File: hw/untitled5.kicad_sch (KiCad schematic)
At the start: 1 part, among them U6 TS3USB3031

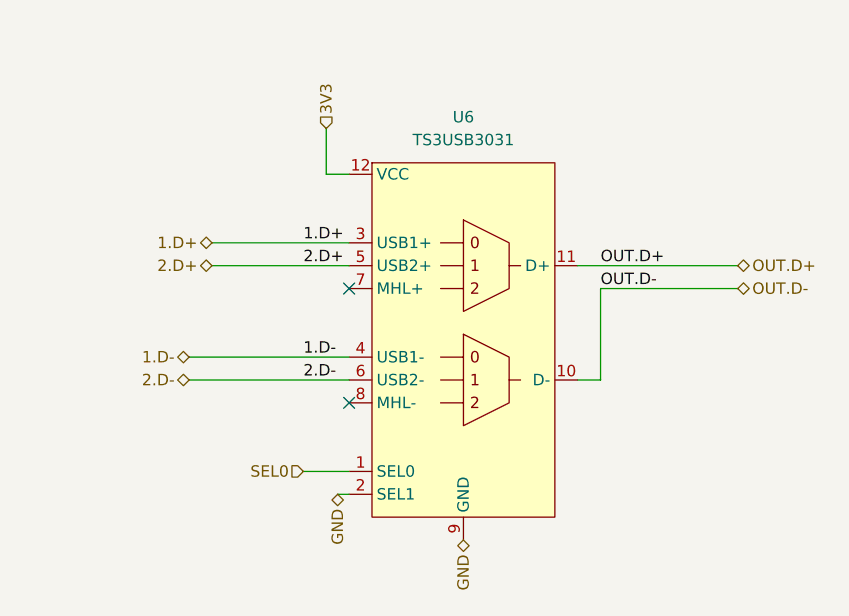
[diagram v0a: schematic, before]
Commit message: Graphic modifications of the scheme
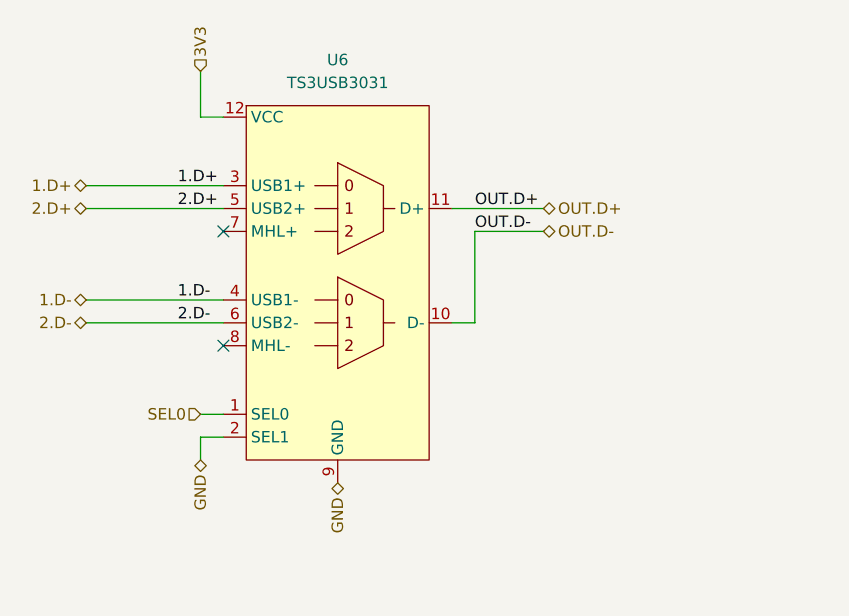
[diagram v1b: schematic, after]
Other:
- moved on the sheet: U6
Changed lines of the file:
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@@
 (kicad_sch (version 20230121) (generator eeschema)
   (paper "A4")
-  (no_connect (at 156.21 87.63))
-  (no_connect (at 156.21 100.33))
-  (wire (pts (xy 140.97 85.09) (xy 156.21 85.09))
+  (no_connect (at 142.24 81.28))
+  (no_connect (at 142.24 93.98))
+  (wire (pts (xy 139.7 106.68) (xy 139.7 104.14))
     (stroke (width 0) (type default))
   )
-  (wire (pts (xy 156.21 74.93) (xy 153.67 74.93))
+  (wire (pts (xy 127 78.74) (xy 142.24 78.74))
     (stroke (width 0) (type default))
   )
-  (wire (pts (xy 154.94 110.49) (xy 156.21 110.49))
+  (wire (pts (xy 142.24 68.58) (xy 139.7 68.58))
     (stroke (width 0) (type default))
   )
-  (wire (pts (xy 138.43 97.79) (xy 156.21 97.79))
+  (wire (pts (xy 127 91.44) (xy 142.24 91.44))
     (stroke (width 0) (type default))
   )
-  (wire (pts (xy 181.61 85.09) (xy 199.39 85.09))
+  (wire (pts (xy 167.64 78.74) (xy 177.8 78.74))
     (stroke (width 0) (type default))
   )
-  (wire (pts (xy 184.15 87.63) (xy 199.39 87.63))
+  (wire (pts (xy 139.7 104.14) (xy 142.24 104.14))
     (stroke (width 0) (type default))
   )
-  (wire (pts (xy 181.61 97.79) (xy 184.15 97.79))
+  (wire (pts (xy 170.18 81.28) (xy 177.8 81.28))
     (stroke (width 0) (type default))
   )
-  (wire (pts (xy 151.13 107.95) (xy 156.21 107.95))
+  (wire (pts (xy 167.64 91.44) (xy 170.18 91.44))
     (stroke (width 0) (type default))
   )
-  (wire (pts (xy 138.43 95.25) (xy 156.21 95.25))
+  (wire (pts (xy 139.7 101.6) (xy 142.24 101.6))
     (stroke (width 0) (type default))
   )
-  (wire (pts (xy 184.15 97.79) (xy 184.15 87.63))
+  (wire (pts (xy 127 88.9) (xy 142.24 88.9))
     (stroke (width 0) (type default))
   )
-  (wire (pts (xy 140.97 82.55) (xy 156.21 82.55))
+  (wire (pts (xy 170.18 91.44) (xy 170.18 81.28))
     (stroke (width 0) (type default))
   )
-  (wire (pts (xy 153.67 69.85) (xy 153.67 74.93))
+  (wire (pts (xy 127 76.2) (xy 142.24 76.2))
     (stroke (width 0) (type default))
   )
-  (label "1.D+" (at 151.13 82.55 0) (fields_autoplaced)
+  (wire (pts (xy 139.7 63.5) (xy 139.7 68.58))
+    (stroke (width 0) (type default))
+  )
+  (label "1.D+" (at 137.16 76.2 0) (fields_autoplaced)
     (effects (font (size 1.27 1.27)) (justify left bottom))
   )
-  (label "1.D-" (at 151.13 95.25 0) (fields_autoplaced)
+  (label "1.D-" (at 137.16 88.9 0) (fields_autoplaced)
     (effects (font (size 1.27 1.27)) (justify left bottom))
   )
-  (label "OUT.D-" (at 184.15 87.63 0) (fields_autoplaced)
+  (label "OUT.D-" (at 170.18 81.28 0) (fields_autoplaced)
     (effects (font (size 1.27 1.27)) (justify left bottom))
   )
-  (label "2.D-" (at 151.13 97.79 0) (fields_autoplaced)
+  (label "2.D-" (at 137.16 91.44 0) (fields_autoplaced)
     (effects (font (size 1.27 1.27)) (justify left bottom))
   )
-  (label "OUT.D+" (at 184.15 85.09 0) (fields_autoplaced)
+  (label "OUT.D+" (at 170.18 78.74 0) (fields_autoplaced)
     (effects (font (size 1.27 1.27)) (justify left bottom))
   )
-  (label "2.D+" (at 151.13 85.09 0) (fields_autoplaced)
+  (label "2.D+" (at 137.16 78.74 0) (fields_autoplaced)
     (effects (font (size 1.27 1.27)) (justify left bottom))
   )
-  (hierarchical_label "2.D-" (shape bidirectional) (at 138.43 97.79 180) (fields_autoplaced)
+  (hierarchical_label "2.D-" (shape bidirectional) (at 127 91.44 180) (fields_autoplaced)
     (effects (font (size 1.27 1.27)) (justify right))
   )
-  (hierarchical_label "3V3" (shape input) (at 153.67 69.85 90) (fields_autoplaced)
+  (hierarchical_label "3V3" (shape input) (at 139.7 63.5 90) (fields_autoplaced)
     (effects (font (size 1.27 1.27)) (justify left))
   )
-  (hierarchical_label "1.D-" (shape bidirectional) (at 138.43 95.25 180) (fields_autoplaced)
+  (hierarchical_label "1.D-" (shape bidirectional) (at 127 88.9 180) (fields_autoplaced)
     (effects (font (size 1.27 1.27)) (justify right))
   )
-  (hierarchical_label "2.D+" (shape bidirectional) (at 140.97 85.09 180) (fields_autoplaced)
+  (hierarchical_label "2.D+" (shape bidirectional) (at 127 78.74 180) (fields_autoplaced)
     (effects (font (size 1.27 1.27)) (justify right))
   )
-  (hierarchical_label "GND" (shape bidirectional) (at 168.91 115.57 270) (fields_autoplaced)
+  (hierarchical_label "GND" (shape bidirectional) (at 154.94 109.22 270) (fields_autoplaced)
     (effects (font (size 1.27 1.27)) (justify right))
   )
-  (hierarchical_label "OUT.D+" (shape bidirectional) (at 199.39 85.09 0) (fields_autoplaced)
+  (hierarchical_label "OUT.D+" (shape bidirectional) (at 177.8 78.74 0) (fields_autoplaced)
     (effects (font (size 1.27 1.27)) (justify left))
   )
-  (hierarchical_label "1.D+" (shape bidirectional) (at 140.97 82.55 180) (fields_autoplaced)
+  (hierarchical_label "1.D+" (shape bidirectional) (at 127 76.2 180) (fields_autoplaced)
     (effects (font (size 1.27 1.27)) (justify right))
   )
-  (hierarchical_label "GND" (shape bidirectional) (at 154.94 110.49 270) (fields_autoplaced)
+  (hierarchical_label "GND" (shape bidirectional) (at 139.7 106.68 270) (fields_autoplaced)
     (effects (font (size 1.27 1.27)) (justify right))
   )
-  (hierarchical_label "SEL0" (shape input) (at 151.13 107.95 180) (fields_autoplaced)
+  (hierarchical_label "SEL0" (shape input) (at 139.7 101.6 180) (fields_autoplaced)
     (effects (font (size 1.27 1.27)) (justify right))
   )
-  (hierarchical_label "OUT.D-" (shape bidirectional) (at 199.39 87.63 0) (fields_autoplaced)
+  (hierarchical_label "OUT.D-" (shape bidirectional) (at 177.8 81.28 0) (fields_autoplaced)
     (effects (font (size 1.27 1.27)) (justify left))
   )
-  (symbol (lib_id "RKL-DiscreteLogic:TS3USB3031") (at 168.91 74.93 0) (unit 1)
+  (symbol (lib_id "RKL-DiscreteLogic:TS3USB3031") (at 154.94 68.58 0) (unit 1)
     (in_bom yes) (on_board yes) (dnp no)
-    (property "Reference" "U6" (at 168.91 68.58 0)
+    (property "Reference" "U6" (at 154.94 62.23 0)
       (effects (font (size 1.27 1.27)))
     )
-    (property "Value" "TS3USB3031" (at 168.91 71.12 0)
+    (property "Value" "TS3USB3031" (at 154.94 64.77 0)
       (effects (font (size 1.27 1.27)))
     )
-    (property "Footprint" "Package_DFN_QFN:Texas_X2QFN-12_1.6x1.6mm_P0.4mm" (at 168.91 66.04 0)
+    (property "Footprint" "Package_DFN_QFN:Texas_X2QFN-12_1.6x1.6mm_P0.4mm" (at 154.94 59.69 0)
       (effects (font (size 1.27 1.27)) hide)
     )
-    (property "Datasheet" "https://www.ti.com/lit/ds/symlink/ts3usb3031.pdf?ts=1703029289212&ref_url=https%253A%252F%252Fwww.google.com%252F" (at 168.91 63.5 0)
+    (property "Datasheet" "https://www.ti.com/lit/ds/symlink/ts3usb3031.pdf?ts=1703029289212&ref_url=https%253A%252F%252Fwww.google.com%252F" (at 154.94 57.15 0)
       (effects (font (size 1.27 1.27)) hide)
     )
-    (property "Basic/Extended" "E" (at 168.91 74.93 0)
+    (property "Basic/Extended" "E" (at 154.94 68.58 0)
       (effects (font (size 1.27 1.27)) hide)
     )
-    (property "LCSC" "C2652459" (at 168.91 74.93 0)
+    (property "LCSC" "C2652459" (at 154.94 68.58 0)
       (effects (font (size 1.27 1.27)) hide)
     )

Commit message: add routing
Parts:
- added C2: 4.7u, Capacitor_SMD:C_0603_1608Metric, symbol Device:C
- added C29: 10u, Capacitor_SMD:C_0603_1608Metric, symbol Device:C
- added R40: 10k, Resistor_SMD:R_0402_1005Metric, symbol Device:R
- added R41: 56k, Resistor_SMD:R_0402_1005Metric, symbol Device:R
- added U2: LD39200, Package_DFN_QFN:DFN-8-1EP_4x4mm_P0.8mm_EP2.3x3.24mm, symbol Robotarna_KiCad_Library:LD39200
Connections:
- net GND: now also C2.2, C29.2, R40.1, U2.4 (GND), U2.9 (GND)
- net 3V3: no longer names the net of U6.12 (VCC)
- net 3V3: now also C29.1, R41.2, U2.1 (OUT), U2.2 (OUT)
- new net: R40.2, R41.1, U2.3 (ADJ/SENSE)
- new net IN: C2.1, U2.6 (EN), U2.7 (IN), U2.8 (IN)
- no-connect marks 2 -> 3

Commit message: Component inspection wip 0
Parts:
- C29: Basic/Extended (none) -> B; LCSC C19702 -> C96446; info (none) -> 25V, X5R
- R40: Basic/Extended (none) -> B
- U2: symbol Robotarna_KiCad_Library:LD39200 -> RKL-LDO:LD39200
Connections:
- net IN renamed VCC
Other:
- moved on the sheet: C2, C29, R40, R41, U2, U6

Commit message: Inspection of parts complete
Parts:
- removed R40: 10k, Resistor_SMD:R_0402_1005Metric, symbol Device:R
- removed R41: 56k, Resistor_SMD:R_0402_1005Metric, symbol Device:R
- removed U2: LD39200, Package_DFN_QFN:DFN-8-1EP_4x4mm_P0.8mm_EP2.3x3.24mm, symbol RKL-LDO:LD39200
- added U11: NCP708, RKL-StandardPackages:UDFN6-3x3mm, symbol RKL-LDO:NCP708
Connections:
- net GND: now also U11.2 (GND), U11.7 (GND)
- net at C29.1, U6.12 (VCC): now also U11.4 (Vout), U11.5 (SNS)
- net VCC renamed VUSB
- net VUSB: now also U11.1 (EN), U11.6 (Vin)
- no-connect marks 3 -> 2
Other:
- moved on the sheet: C2

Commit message: Solved issue "Micro USB"
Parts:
- U11: JLCPCB_CORRECTION 0;0;-90 -> 0;0;180
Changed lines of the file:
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@@
       (effects (font (size 1.27 1.27)) hide)
     )
-    (property "JLCPCB_CORRECTION" "0;0;-90" (at 127 55.245 0)
+    (property "JLCPCB_CORRECTION" "0;0;180" (at 127 55.245 0)
       (effects (font (size 1.27 1.27)) hide)
     )
